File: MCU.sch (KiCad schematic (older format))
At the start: 18 parts, among them J1 Conn_01x05, J2 Conn_01x14, U2 STM32F072RBTx

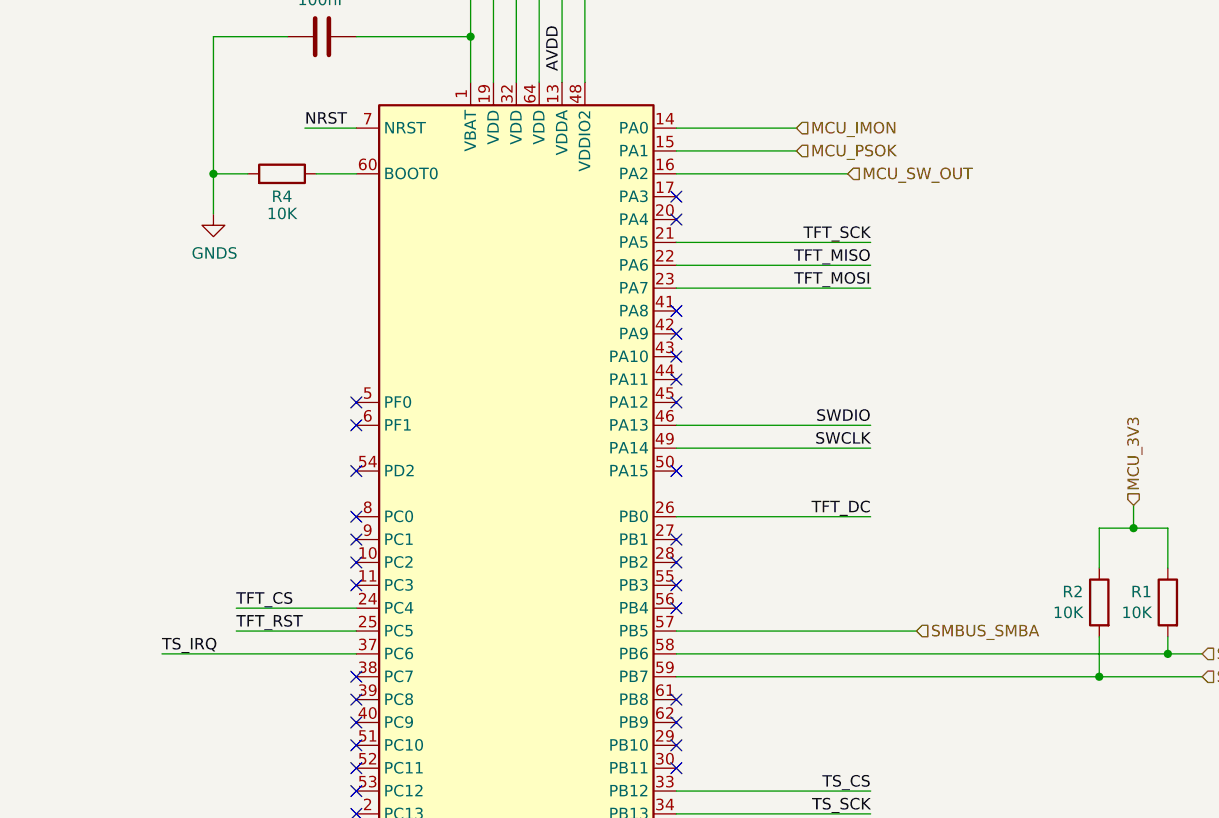
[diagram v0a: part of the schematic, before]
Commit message: Corrected Pin numbering errors :)
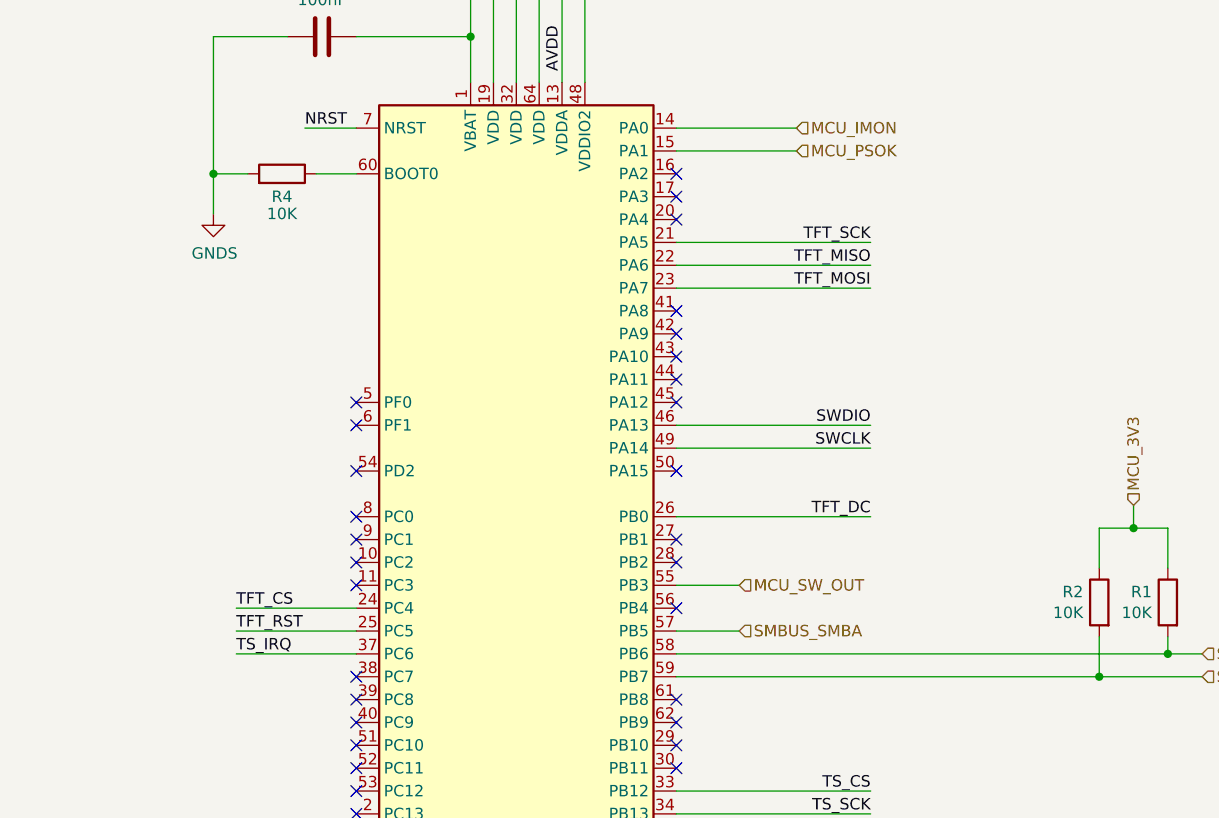
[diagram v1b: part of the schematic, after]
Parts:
- J2: footprint ILI9341_TFTLCD:ILI9341_ResitiveTouch_TFTLCD_2.8inch_85mm_50mm -> ILI9341_TFTLCD:ILI9341_ResitiveTouch_TFTLCD_2.8inch_85mm_50mm_FrontMount
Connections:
- net MCU_SW_OUT: now also U2.55 (PB3); no longer U2.16 (PA2)
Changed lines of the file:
@@
 	9000 7800 8850 7800
 Wire Wire Line
-	6700 7700 7750 7700
-Text HLabel 7750 7700 2    50   Input ~ 0
+	6700 7700 6975 7700
+Text HLabel 6975 7700 2    50   Input ~ 0
 SMBUS_SMBA
 $Comp
@@
 F 0 "J2" H 13805 2892 50  0000 L CNN
 F 1 "Conn_01x14" H 13805 2801 50  0000 L CNN
-F 2 "ILI9341_TFTLCD:ILI9341_ResitiveTouch_TFTLCD_2.8inch_85mm_50mm" H 13725 2900 50  0001 C CNN
+F 2 "ILI9341_TFTLCD:ILI9341_ResitiveTouch_TFTLCD_2.8inch_85mm_50mm_FrontMount" H 13725 2900 50  0001 C CNN
 F 3 "~" H 13725 2900 50  0001 C CNN
 	1    13725 2900
@@
 	6700 8600 7550 8600
 Wire Wire Line
-	5300 7800 4450 7800
+	5300 7800 4775 7800
 Text Label 7550 8500 2    50   ~ 0
 TS_SCK
@@
 Text Label 7550 8600 2    50   ~ 0
 TS_MISO
-Text Label 4450 7800 0    50   ~ 0
+Text Label 4775 7800 0    50   ~ 0
 TS_IRQ
 NoConn ~ 6700 5800
@@
 NoConn ~ 6700 6700
 NoConn ~ 6700 7000
-NoConn ~ 6700 7500
+NoConn ~ 6700 5700
 NoConn ~ 6700 7600
 NoConn ~ 6700 8000
@@
 	11100 7475 11100 7625
 Wire Wire Line
-	6700 5700 7450 5700
-Text HLabel 7450 5700 2    50   Input ~ 0
+	6700 7500 6975 7500
+Text HLabel 6975 7500 2    50   Input ~ 0
 MCU_SW_OUT
 NoConn ~ 5300 8400
